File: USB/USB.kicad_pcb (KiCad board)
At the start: 4 copper layers, 36.9 x 37.9 mm, 46 parts, among them IC1 TXS0202YZPR, IC2 NCV8730ASN330T1G, IC3 TXS0202YZPR, J1 MISC1, U1 TLV61222

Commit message: Fix #7
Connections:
- IC1 pad B2: +3V3 -> +2V5
- IC1 pad C1: +2V5 -> +3V3
- IC1 pad C2: +2V5 -> +3V3
- IC3 pad B2: +3V3 -> +2V5
- IC3 pad C1: +2V5 -> +3V3
- IC3 pad C2: +2V5 -> +3V3
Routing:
- net +2V5: track 33.0 -> 30.3 mm
- net GND: vias 150 -> 161

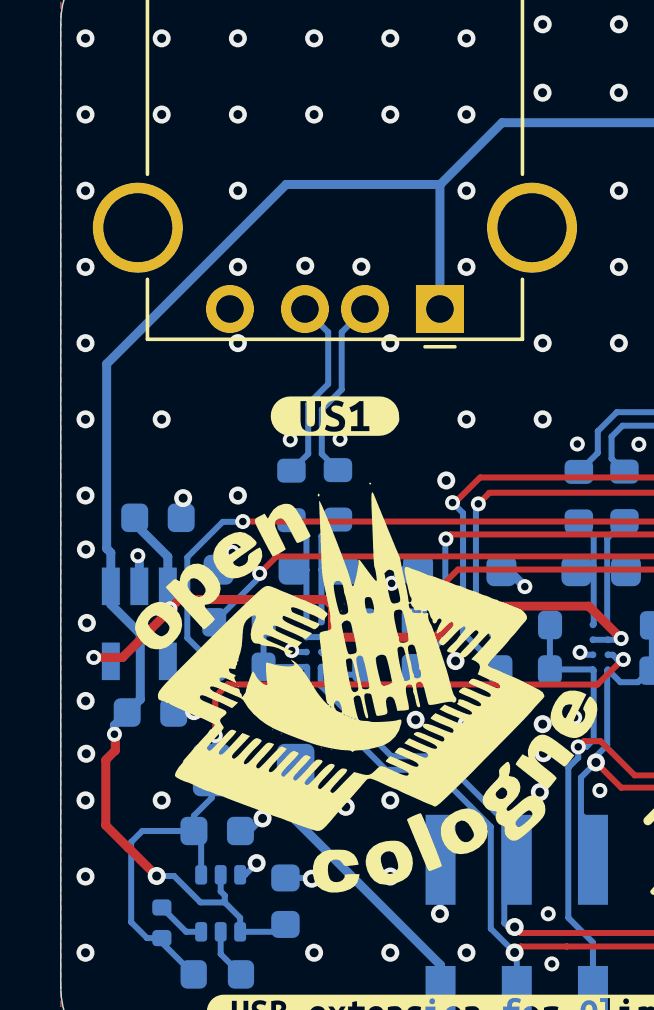
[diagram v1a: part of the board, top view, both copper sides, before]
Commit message: Fix #6
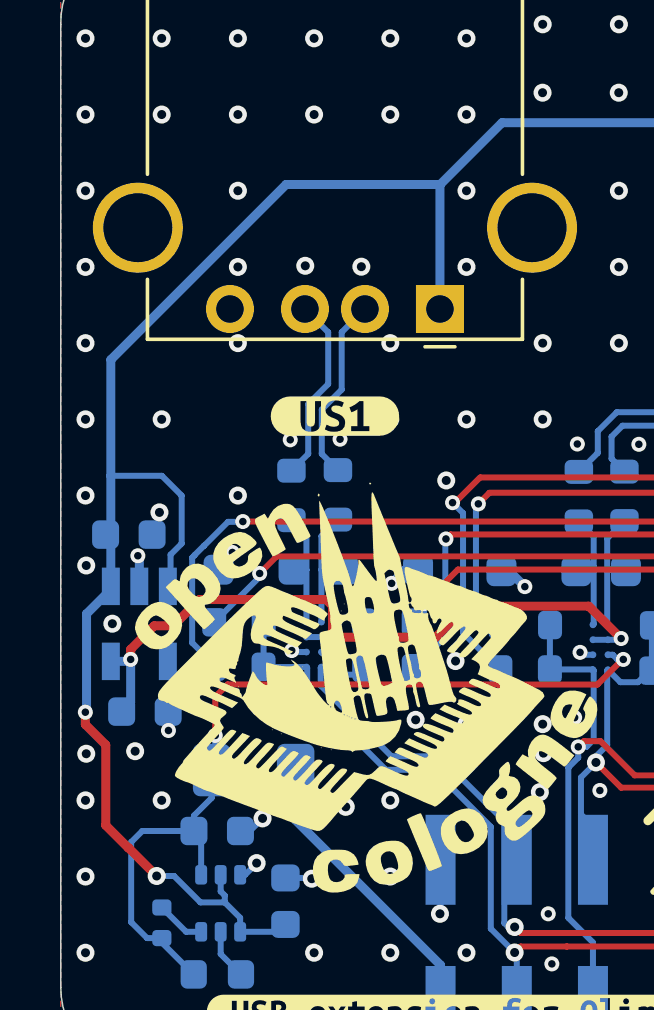
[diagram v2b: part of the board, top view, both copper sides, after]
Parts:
- moved C4 6.47 mm to (86.9, 109.9)
- moved C3 5.97 mm to (86.3, 104.0)
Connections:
- IC2 pad 3: +3V3 -> +5V
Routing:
- net +5V: track 66.5 -> 72.0 mm
- net +3V3: track 26.4 -> 23.8 mm, vias 4 -> 3
